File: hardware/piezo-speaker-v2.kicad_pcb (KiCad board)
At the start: 2 copper layers, 45 x 55 mm, 44 parts, among them P1 CON-SENSOR2, P2 BOOT, P3 DEBUG, P4 PT-4532PLQ, Q101 2N7002P, U1 XMC1100, U2 LD1117-ADJ, U3 LMR62014X, U4 DRILL, U5 DRILL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

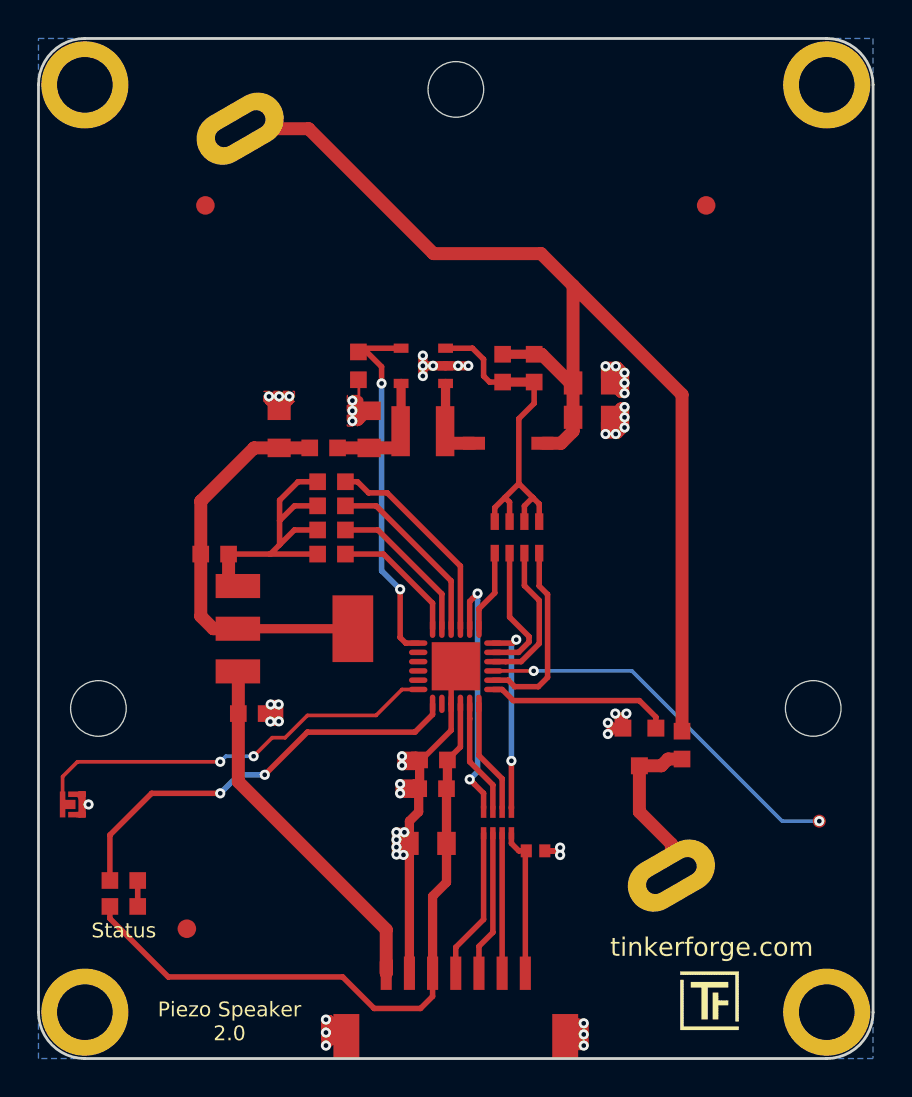
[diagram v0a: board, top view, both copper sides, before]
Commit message: add correct drills
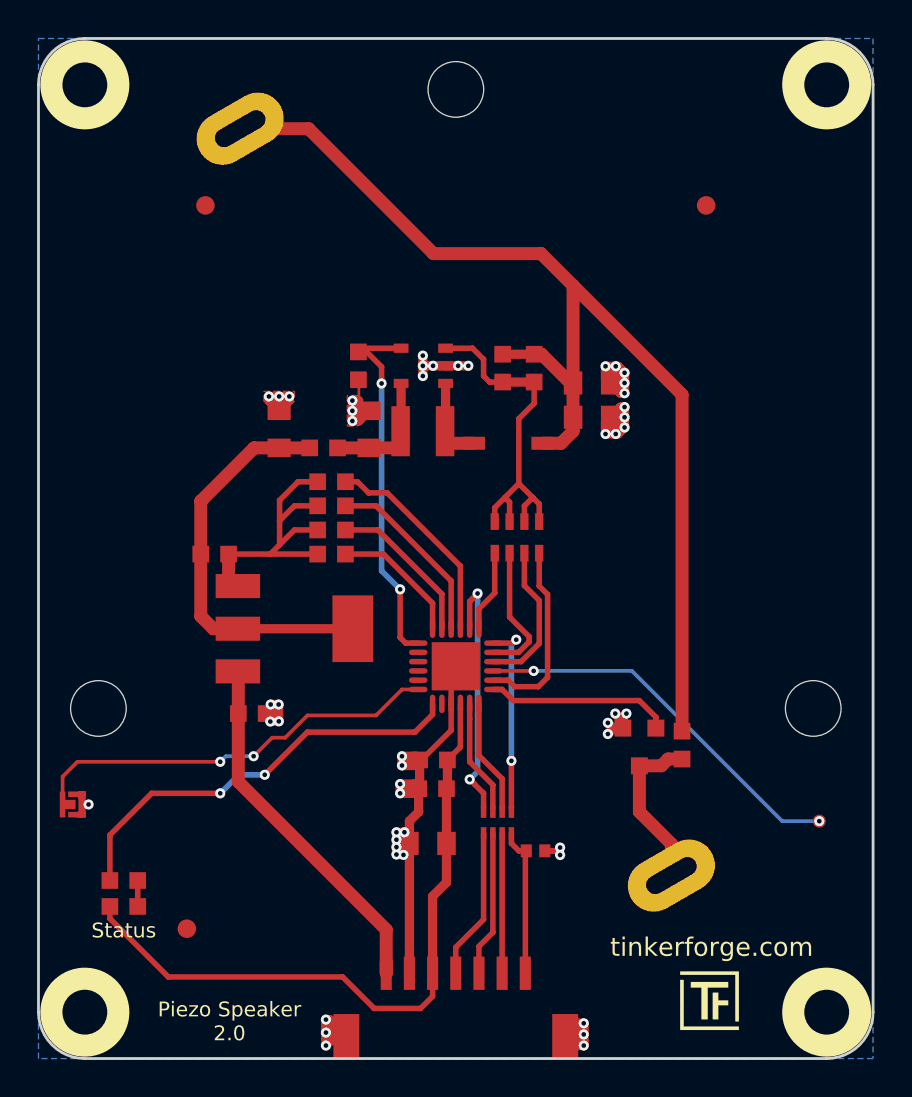
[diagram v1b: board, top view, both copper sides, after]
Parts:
- U4, U5, U6, U7: footprint kicad-libraries:Drill -> kicad-libraries:DRILL_NP
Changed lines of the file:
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@@
     )
-  )
-  (module kicad-libraries:Drill (layer F.Cu)
-    (at 135 127.5)
-    (fp_text reference U4 (at 0 0) (layer F.SilkS) hide
-      (effects (font (size 0.29972 0.29972) (thickness 0.0762)))
-    )
-    (fp_text value DRILL (at 0 0.50038) (layer F.SilkS) hide
-      (effects (font (size 0.29972 0.29972) (thickness 0.0762)))
-    )
-    (pad "" thru_hole circle (at 0 0) (size 4.699 4.699) (drill 2.99974) (layers *.Cu *.SilkS *.Mask))
-  )
-  (module kicad-libraries:Drill (layer F.Cu)
-    (at 175 127.5)
-    (fp_text reference U5 (at 0 0) (layer F.SilkS) hide
-      (effects (font (size 0.29972 0.29972) (thickness 0.0762)))
-    )
-    (fp_text value DRILL (at 0 0.50038) (layer F.SilkS) hide
-      (effects (font (size 0.29972 0.29972) (thickness 0.0762)))
-    )
-    (pad "" thru_hole circle (at 0 0) (size 4.699 4.699) (drill 2.99974) (layers *.Cu *.SilkS *.Mask))
-  )
-  (module kicad-libraries:Drill (layer F.Cu)
-    (at 175 77.5)
-    (fp_text reference U6 (at 0 0) (layer F.SilkS) hide
-      (effects (font (size 0.29972 0.29972) (thickness 0.0762)))
-    )
-    (fp_text value DRILL (at 0 0.50038) (layer F.SilkS) hide
-      (effects (font (size 0.29972 0.29972) (thickness 0.0762)))
-    )
-    (pad "" thru_hole circle (at 0 0) (size 4.699 4.699) (drill 2.99974) (layers *.Cu *.SilkS *.Mask))
-  )
-  (module kicad-libraries:Drill (layer F.Cu)
-    (at 135 77.5)
-    (fp_text reference U7 (at 0 0) (layer F.SilkS) hide
-      (effects (font (size 0.29972 0.29972) (thickness 0.0762)))
-    )
-    (fp_text value DRILL (at 0 0.50038) (layer F.SilkS) hide
-      (effects (font (size 0.29972 0.29972) (thickness 0.0762)))
-    )
-    (pad "" thru_hole circle (at 0 0) (size 4.699 4.699) (drill 2.99974) (layers *.Cu *.SilkS *.Mask))
   )
   (module kicad-libraries:WEEE_7mm (layer B.Cu)
@@
       (clearance 0.65024))
   )
+  (module kicad-libraries:DRILL_NP (layer F.Cu)
+    (at 135 127.5)
+    (fp_text reference U4 (at 0 0) (layer F.SilkS) hide
+      (effects (font (size 0.29972 0.29972) (thickness 0.0762)))
+    )
+    (fp_text value DRILL (at 0 0.50038) (layer F.SilkS) hide
+      (effects (font (size 0.29972 0.29972) (thickness 0.0762)))
+    )
+    (fp_circle (center 0 0) (end 3.2 0) (layer Eco2.User) (width 0.01))
+    (fp_circle (center 0 0) (end 2.19964 -0.20066) (layer F.SilkS) (width 0.381))
+    (fp_circle (center 0 0) (end 1.99898 -0.20066) (layer F.SilkS) (width 0.381))
+    (fp_circle (center 0 0) (end 1.69926 0) (layer F.SilkS) (width 0.381))
+    (fp_circle (center 0 0) (end 1.39954 -0.09906) (layer B.SilkS) (width 0.381))
+    (fp_circle (center 0 0) (end 1.39954 0) (layer F.SilkS) (width 0.381))
+    (fp_circle (center 0 0) (end 1.69926 0) (layer B.SilkS) (width 0.381))
+    (fp_circle (center 0 0) (end 1.89992 0) (layer B.SilkS) (width 0.381))
+    (fp_circle (center 0 0) (end 2.19964 0) (layer B.SilkS) (width 0.381))
+    (pad "" np_thru_hole circle (at 0 0) (size 2.99974 2.99974) (drill 2.99974) (layers *.Cu *.Mask F.SilkS)
+      (clearance 0.89916))
+  )
+  (module kicad-libraries:DRILL_NP (layer F.Cu)
+    (at 175 127.5)
+    (fp_text reference U5 (at 0 0) (layer F.SilkS) hide
+      (effects (font (size 0.29972 0.29972) (thickness 0.0762)))
+    )
+    (fp_text value DRILL (at 0 0.50038) (layer F.SilkS) hide
+      (effects (font (size 0.29972 0.29972) (thickness 0.0762)))
+    )
+    (fp_circle (center 0 0) (end 2.19964 0) (layer B.SilkS) (width 0.381))
+    (fp_circle (center 0 0) (end 1.89992 0) (layer B.SilkS) (width 0.381))
+    (fp_circle (center 0 0) (end 1.69926 0) (layer B.SilkS) (width 0.381))
+    (fp_circle (center 0 0) (end 1.39954 0) (layer F.SilkS) (width 0.381))
+    (fp_circle (center 0 0) (end 1.39954 -0.09906) (layer B.SilkS) (width 0.381))
+    (fp_circle (center 0 0) (end 1.69926 0) (layer F.SilkS) (width 0.381))
+    (fp_circle (center 0 0) (end 1.99898 -0.20066) (layer F.SilkS) (width 0.381))
+    (fp_circle (center 0 0) (end 2.19964 -0.20066) (layer F.SilkS) (width 0.381))
+    (fp_circle (center 0 0) (end 3.2 0) (layer Eco2.User) (width 0.01))
+    (pad "" np_thru_hole circle (at 0 0) (size 2.99974 2.99974) (drill 2.99974) (layers *.Cu *.Mask F.SilkS)
+      (clearance 0.89916))
+  )
+  (module kicad-libraries:DRILL_NP (layer F.Cu)
+    (at 175 77.5)
+    (fp_text reference U6 (at 0 0) (layer F.SilkS) hide
+      (effects (font (size 0.29972 0.29972) (thickness 0.0762)))
+    )
+    (fp_text value DRILL (at 0 0.50038) (layer F.SilkS) hide
+      (effects (font (size 0.29972 0.29972) (thickness 0.0762)))
+    )
+    (fp_circle (center 0 0) (end 3.2 0) (layer Eco2.User) (width 0.01))
+    (fp_circle (center 0 0) (end 2.19964 -0.20066) (layer F.SilkS) (width 0.381))
+    (fp_circle (center 0 0) (end 1.99898 -0.20066) (layer F.SilkS) (width 0.381))
+    (fp_circle (center 0 0) (end 1.69926 0) (layer F.SilkS) (width 0.381))
+    (fp_circle (center 0 0) (end 1.39954 -0.09906) (layer B.SilkS) (width 0.381))
+    (fp_circle (center 0 0) (end 1.39954 0) (layer F.SilkS) (width 0.381))
+    (fp_circle (center 0 0) (end 1.69926 0) (layer B.SilkS) (width 0.381))
+    (fp_circle (center 0 0) (end 1.89992 0) (layer B.SilkS) (width 0.381))
+    (fp_circle (center 0 0) (end 2.19964 0) (layer B.SilkS) (width 0.381))
+    (pad "" np_thru_hole circle (at 0 0) (size 2.99974 2.99974) (drill 2.99974) (layers *.Cu *.Mask F.SilkS)
+      (clearance 0.89916))
+  )
+  (module kicad-libraries:DRILL_NP (layer F.Cu)
+    (at 135 77.5)
+    (fp_text reference U7 (at 0 0) (layer F.SilkS) hide
+      (effects (font (size 0.29972 0.29972) (thickness 0.0762)))
+    )
+    (fp_text value DRILL (at 0 0.50038) (layer F.SilkS) hide
+      (effects (font (size 0.29972 0.29972) (thickness 0.0762)))
+    )
+    (fp_circle (center 0 0) (end 3.2 0) (layer Eco2.User) (width 0.01))
+    (fp_circle (center 0 0) (end 2.19964 -0.20066) (layer F.SilkS) (width 0.381))
+    (fp_circle (center 0 0) (end 1.99898 -0.20066) (layer F.SilkS) (width 0.381))
+    (fp_circle (center 0 0) (end 1.69926 0) (layer F.SilkS) (width 0.381))
+    (fp_circle (center 0 0) (end 1.39954 -0.09906) (layer B.SilkS) (width 0.381))
+    (fp_circle (center 0 0) (end 1.39954 0) (layer F.SilkS) (width 0.381))
+    (fp_circle (center 0 0) (end 1.69926 0) (layer B.SilkS) (width 0.381))
+    (fp_circle (center 0 0) (end 1.89992 0) (layer B.SilkS) (width 0.381))
+    (fp_circle (center 0 0) (end 2.19964 0) (layer B.SilkS) (width 0.381))
+    (pad "" np_thru_hole circle (at 0 0) (size 2.99974 2.99974) (drill 2.99974) (layers *.Cu *.Mask F.SilkS)
+      (clearance 0.89916))
+  )
   (gr_circle (center 155 100) (end 167 100) (layer Dwgs.User) (width 0.2))
